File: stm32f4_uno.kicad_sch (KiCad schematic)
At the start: 48 parts, among them J1 Barrel_Jack, J101 Digital/PWM, J102 Power, J103 Analog, J104 Digital/PWM, J106 Ethernet, J107 STM32 GPIO, J108 STM32 GPIO, J109 STM32 GPIO, J110 STM32 GPIO, J111 STM32 GPIO, J4 Conn_ST_STDC14, U101 STM32F407VGTx, Y3 32.768kHz, Y4 25MHz

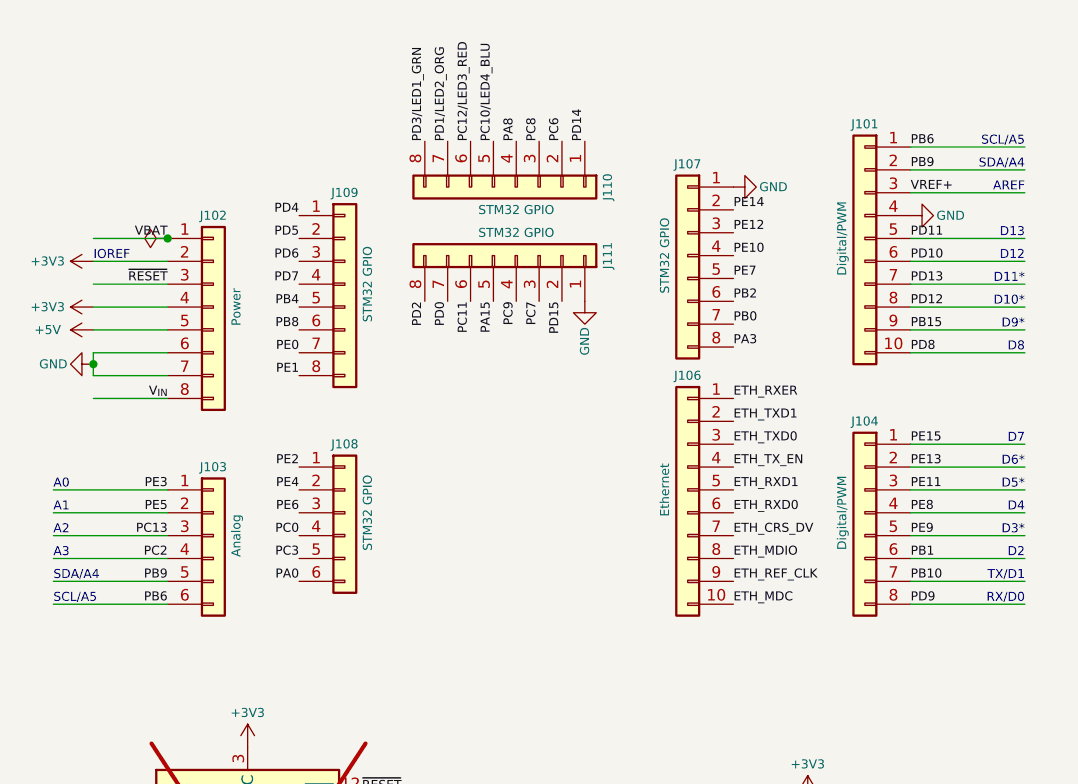
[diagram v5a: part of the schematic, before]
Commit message: Replace 3V3 LDO for a 1A model
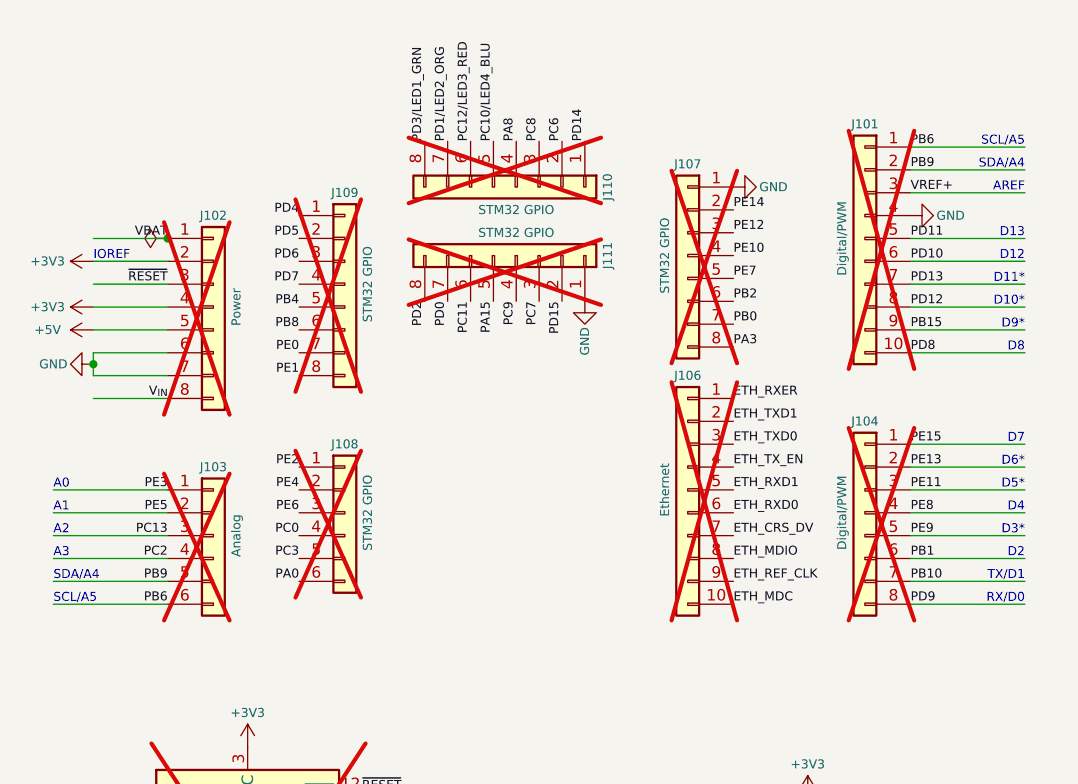
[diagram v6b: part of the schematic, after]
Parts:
- J101, J102, J103, J104, J106, J107, J108, J109, J110, J111: now not fitted

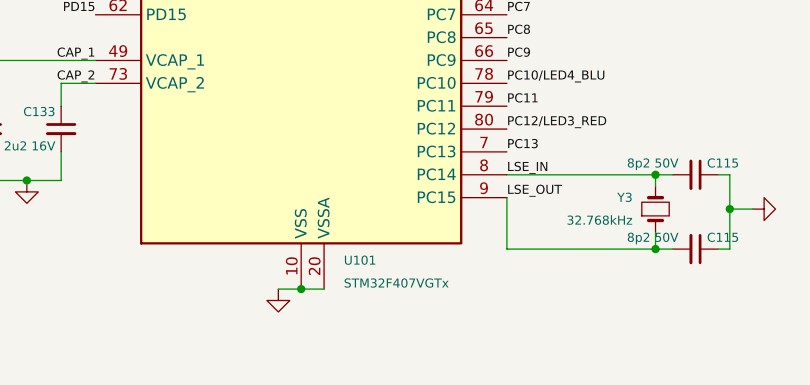
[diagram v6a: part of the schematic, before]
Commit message: Set DNP on devices not to populate
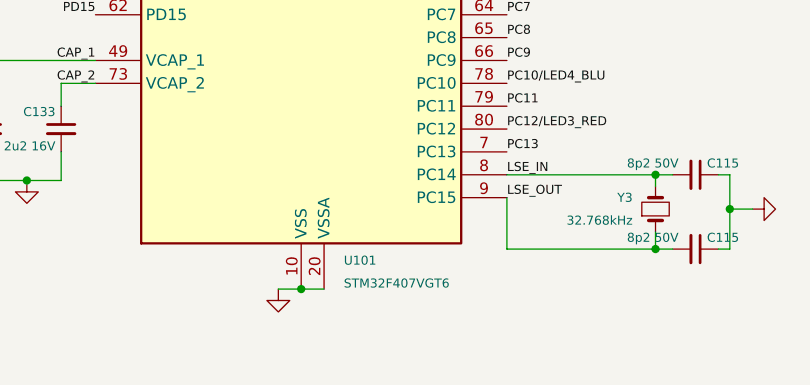
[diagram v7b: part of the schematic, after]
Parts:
- J1, J101, J102, J103, J104, J106, J107, J108, J109, J110, J111: now left out of the parts list
- U101: value STM32F407VGTx -> STM32F407VGT6; JLCPCB Part # (none) -> C12345; Manufacturer (none) -> STMicroelectronics; Partnumber (none) -> STM32F407VGT6; isBasicPart (none) -> NO
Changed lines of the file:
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@@
   )
   (symbol (lib_id "Connector_Generic:Conn_01x08") (at 189.865 45.085 0) (unit 1)
-    (in_bom yes) (on_board yes) (dnp yes)
+    (in_bom no) (on_board yes) (dnp yes)
     (property "Reference" "J102" (at 189.865 34.925 0)
       (effects (font (size 1 1)))
@@
   )
   (symbol (lib_id "Connector_Generic:Conn_01x10") (at 262.255 37.465 0) (mirror y) (unit 1)
-    (in_bom yes) (on_board yes) (dnp yes)
+    (in_bom no) (on_board yes) (dnp yes)
     (property "Reference" "J101" (at 262.255 24.765 0)
       (effects (font (size 1 1)))
@@
   )
   (symbol (lib_id "Connector_Generic:Conn_01x06") (at 189.865 70.485 0) (unit 1)
-    (in_bom yes) (on_board yes) (dnp yes)
+    (in_bom no) (on_board yes) (dnp yes)
     (property "Reference" "J103" (at 189.865 62.865 0)
       (effects (font (size 1 1)))
@@
   )
   (symbol (lib_id "Connector_Generic:Conn_01x08") (at 262.255 67.945 0) (mirror y) (unit 1)
-    (in_bom yes) (on_board yes) (dnp yes)
+    (in_bom no) (on_board yes) (dnp yes)
     (property "Reference" "J104" (at 262.255 57.785 0)
       (effects (font (size 1 1)))
@@
   )
   (symbol (lib_id "Connector_Generic:Conn_01x08") (at 223.52 31.75 270) (unit 1)
-    (in_bom yes) (on_board yes) (dnp yes)
+    (in_bom no) (on_board yes) (dnp yes)
     (property "Reference" "J110" (at 233.68 31.75 0)
       (effects (font (size 1 1)))
@@
   )
   (symbol (lib_id "Connector:Barrel_Jack_Switch") (at 165.1 147.32 0) (unit 1)
-    (in_bom yes) (on_board yes) (dnp yes) (fields_autoplaced)
+    (in_bom no) (on_board yes) (dnp yes) (fields_autoplaced)
     (property "Reference" "J1" (at 165.1 139.065 0)
       (effects (font (size 1.27 1.27)))
@@
   )
   (symbol (lib_id "Connector_Generic:Conn_01x10") (at 242.57 65.405 0) (mirror y) (unit 1)
-    (in_bom yes) (on_board yes) (dnp yes)
+    (in_bom no) (on_board yes) (dnp yes)
     (property "Reference" "J106" (at 242.57 52.705 0)
       (effects (font (size 1 1)))
@@
   )
   (symbol (lib_id "Connector_Generic:Conn_01x08") (at 242.57 39.37 0) (mirror y) (unit 1)
-    (in_bom yes) (on_board yes) (dnp yes)
+    (in_bom no) (on_board yes) (dnp yes)
     (property "Reference" "J107" (at 242.57 29.21 0)
       (effects (font (size 1 1)))
@@
   )
   (symbol (lib_id "Connector_Generic:Conn_01x08") (at 223.52 39.37 270) (mirror x) (unit 1)
-    (in_bom yes) (on_board yes) (dnp yes)
+    (in_bom no) (on_board yes) (dnp yes)
     (property "Reference" "J111" (at 233.68 39.37 0)
       (effects (font (size 1 1)))
@@
   )
   (symbol (lib_id "Connector_Generic:Conn_01x08") (at 204.47 42.545 0) (unit 1)
-    (in_bom yes) (on_board yes) (dnp yes)
+    (in_bom no) (on_board yes) (dnp yes)
     (property "Reference" "J109" (at 204.47 32.385 0)
       (effects (font (size 1 1)))
@@
       (effects (font (size 1 1)) (justify left))
     )
-    (property "Value" "STM32F407VGTx" (at 88.5541 171.45 0)
+    (property "Value" "STM32F407VGT6" (at 88.5541 171.45 0)
       (effects (font (size 1 1)) (justify left))
     )
@@
       (effects (font (size 1 1)) hide)
     )
+    (property "Description" "1MB 1.8V~3.6V ARM Cortex-M4 192KB 168MHz FLASH 82 LQFP-100(14x14)  Microcontroller Units (MCUs/MPUs/SOCs) ROHS" (at 83.82 100.965 0)
+      (effects (font (size 1.27 1.27)) hide)
+    )
+    (property "Manufacturer" "STMicroelectronics" (at 83.82 100.965 0)
+      (effects (font (size 1.27 1.27)) hide)
+    )
+    (property "Partnumber" "STM32F407VGT6" (at 83.82 100.965 0)
+      (effects (font (size 1.27 1.27)) hide)
+    )
+    (property "JLCPCB Part #" "C12345" (at 83.82 100.965 0)
+      (effects (font (size 1.27 1.27)) hide)
+    )
+    (property "isBasicPart" "NO" (at 83.82 100.965 0)
+      (effects (font (size 1.27 1.27)) hide)
+    )
     (pin "1")
     (pin "10")
@@
   )
   (symbol (lib_id "Connector_Generic:Conn_01x06") (at 204.47 67.945 0) (unit 1)
-    (in_bom yes) (on_board yes) (dnp yes)
+    (in_bom no) (on_board yes) (dnp yes)
     (property "Reference" "J108" (at 204.47 60.325 0)
       (effects (font (size 1 1)))

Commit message: #1 Use new central library KiCad-Lib
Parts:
- J4: footprint Project_Library:Samtec_FTSH-107-XX-YYY-DV-K -> #Connector_Debug:Amphenol ICC 20021511-00014T4LF; symbol Connector:Conn_ST_STDC14 -> #Connector_Debug:Conn_ST_STDC14; now in the parts list
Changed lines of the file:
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@@
     )
   )
-  (symbol (lib_id "Connector:Conn_ST_STDC14") (at 193.675 111.76 0) (unit 1)
-    (in_bom no) (on_board yes) (dnp yes)
+  (symbol (lib_id "#Connector_Debug:Conn_ST_STDC14") (at 193.675 111.76 0) (unit 1)
+    (in_bom yes) (on_board yes) (dnp yes)
     (property "Reference" "J4" (at 179.07 104.14 90)
       (effects (font (size 1 1)) (justify right))
@@
       (effects (font (size 1 1)) (justify right))
     )
-    (property "Footprint" "Project_Library:Samtec_FTSH-107-XX-YYY-DV-K" (at 193.675 111.76 0)
-      (effects (font (size 1 1)) hide)
+    (property "Footprint" "#Connector_Debug:Amphenol ICC 20021511-00014T4LF" (at 193.675 111.76 0)
+      (effects (font (size 1.27 1.27)) hide)
     )
-    (property "Datasheet" "https://www.st.com/content/ccc/resource/technical/document/user_manual/group1/99/49/91/b6/b2/3a/46/e5/DM00526767/files/DM00526767.pdf/jcr:content/translations/en.DM00526767.pdf" (at 184.785 143.51 90)
-      (effects (font (size 1 1)) hide)
+    (property "Datasheet" "${KIPRJMOD}/KiCad-Lib/#Connector.doc/Conn_ST_STDC14.pdf" (at 184.785 143.51 90)
+      (effects (font (size 1.27 1.27)) hide)
     )
     (property "Manufacturer" "Samtec" (at 193.675 111.76 0)
